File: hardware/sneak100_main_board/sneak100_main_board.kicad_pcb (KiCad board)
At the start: 2 copper layers, 68 x 72 mm, 106 parts, among them J1 Conn_01x06, J10 Conn_01x03, J11 USB_OTG, J12 Conn_01x06, J13 Conn_02x02_Odd_Even, J2 Conn_01x06, J3 Conn_01x06, J4 Conn_01x06, J5 Conn_01x03, J6 Conn_01x02, J7 Conn_01x03, J8 Conn_01x03, J9 Conn_01x03, Q1 Q_PMOS_DGS, Q2 Q_PMOS_DGS, Q3 SFH-313FA, Q4 SFH-313FA, Q5 SFH-313FA, Q6 SFH-313FA, SW1 SW_Push_SPDT, SW2 SW_Push, SW3 SW_Push, SW4 SW_Push, U1 DRV8835, U2 DRV8835, U3 DRV8835, U4 DRV8835, U5 LM1117-3.3, U6 CD4051B, U7 CD4051B, U8 TSOP4838, U9 STM32F405RGTx, Y1 8MHz

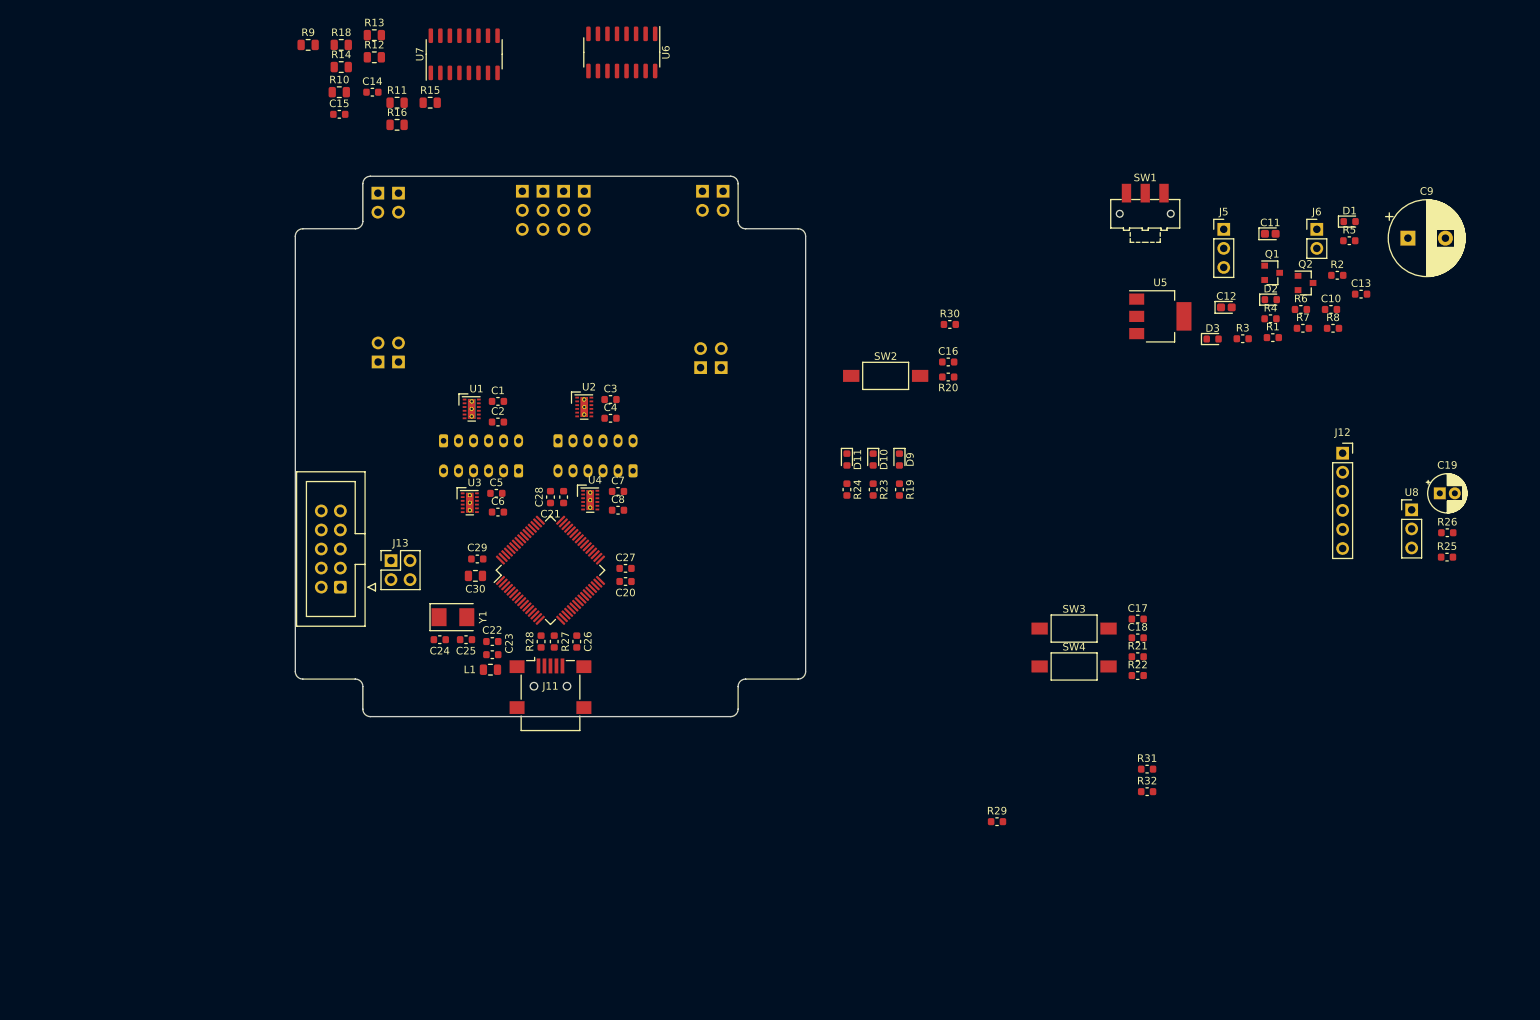
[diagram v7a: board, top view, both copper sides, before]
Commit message: delete USB, modify top hull, bigger PCB board
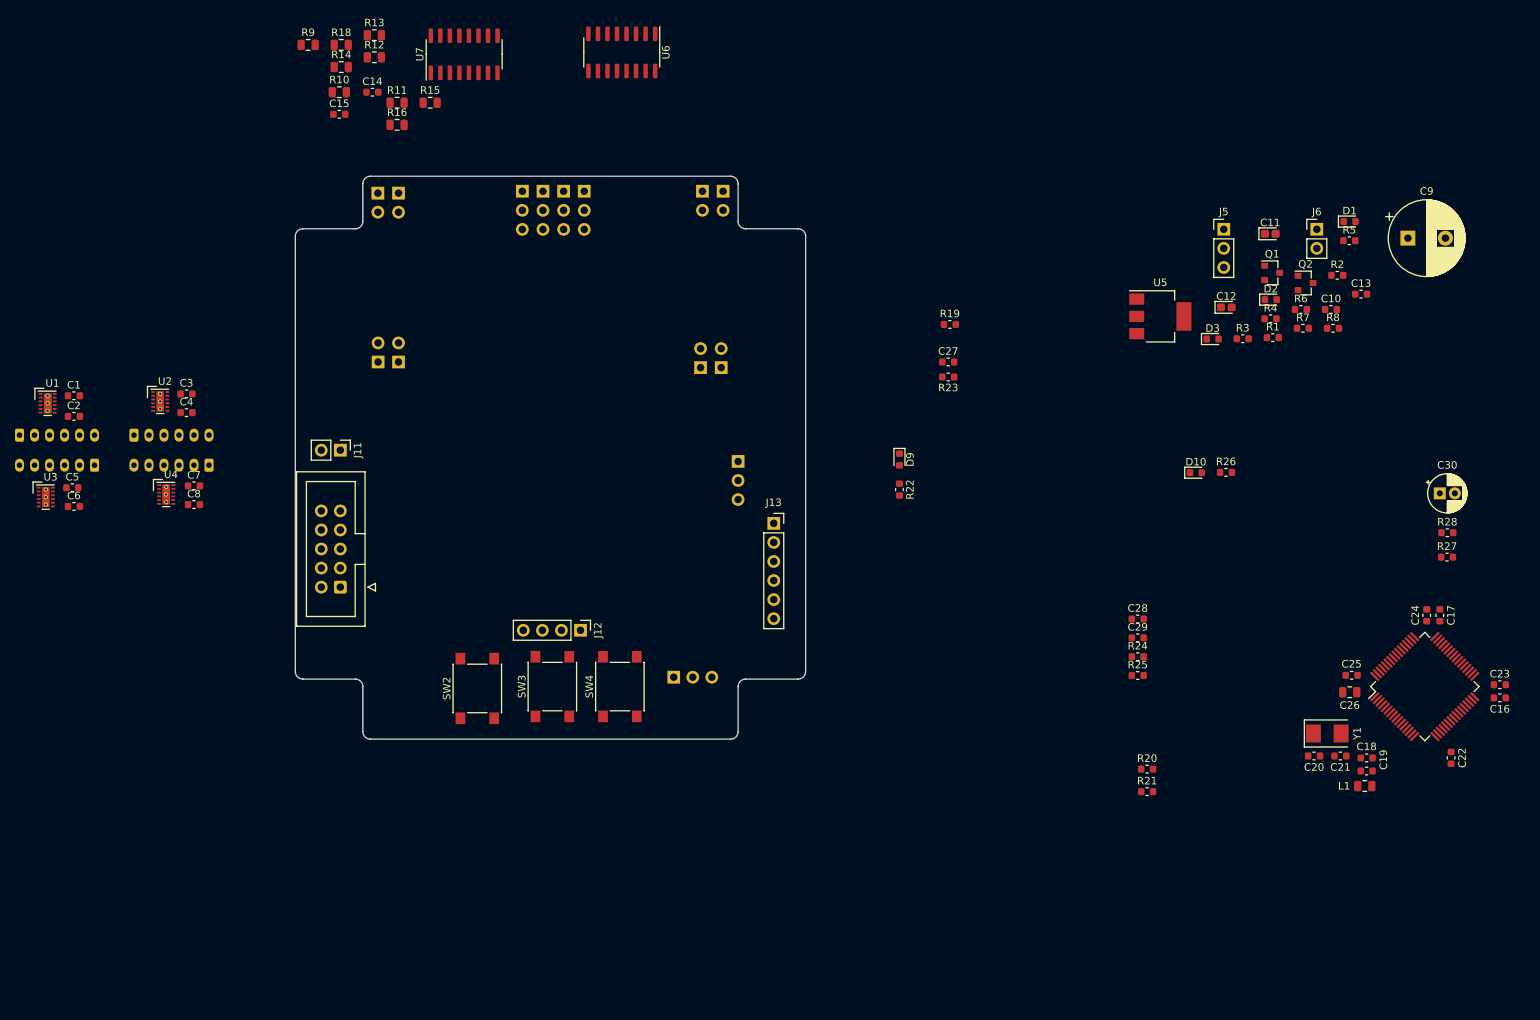
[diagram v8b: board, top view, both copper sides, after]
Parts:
- removed D11: LED, LED_SMD:LED_0603_1608Metric
- removed the J13 at (126.5, 92.7)
- removed the R23 at (190.8, 83.2)
- removed the R24 at (187.2, 83.2)
- removed the R27 at (148.2, 103.5)
- removed the R28 at (146.5, 103.5)
- removed R29: 4k7, Resistor_SMD:R_0603_1608Metric
- added J12: Conn_01x04, Connector_PinHeader_2.54mm:PinHeader_1x04_P2.54mm_Vertical, F.Cu at (151.8, 102.0)
- added R26: 340, Resistor_SMD:R_0603_1608Metric, F.Cu at (237.8, 81.0)
- J11: value USB_OTG -> Conn_01x02; footprint Connector_USB:USB_Mini-B_Lumberg_2486_01_Horizontal -> Connector_PinHeader_2.54mm:PinHeader_1x02_P2.54mm_Vertical
- SW1: footprint Button_Switch_SMD:SW_SPDT_CK-JS102011SAQN -> Connector_PinHeader_2.54mm:PinHeader_1x03_P2.54mm_Vertical; moved to B.Cu
- SW2, SW3, SW4: footprint Button_Switch_SMD:SW_SPST_FSMSM -> Button_Switch_SMD:SW_Push_1P1T_NO_6x6mm_H9.5mm
- U9: renamed from U8; moved to B.Cu
- moved C17 117.8 mm to (266.2, 100.0)
- moved C24 117.8 mm to (264.5, 100.0)
- moved C16 117.5 mm to (274.2, 111.0)
- moved C18 117.5 mm to (256.5, 119.0)
- moved C19 117.5 mm to (256.5, 120.8)
- moved C20 117.5 mm to (249.5, 118.8)
- moved C21 117.5 mm to (253.0, 118.8)
- moved C22 117.5 mm to (267.8, 119.0)
- moved C23 117.5 mm to (274.2, 109.2)
- moved C25 117.5 mm to (254.5, 108.0)
- moved C26 117.5 mm to (254.2, 110.2)
- moved L1 117.5 mm to (256.2, 122.8)
- moved U8 117.5 mm to (264.2, 109.5)
- moved Y1 117.5 mm to (251.2, 115.8)
- moved U9 90.0 mm to (172.8, 79.5), turned to 180 degrees
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- renumbered C20 to C16, C21 to C17, C22 to C18, C23 to C19, C24 to C20, C25 to C21, C26 to C22, C27 to C23, C28 to C24, C29 to C25, C30 to C26, C16 to C27, C17 to C28, C18 to C29, C19 to C30, J12 to J13, R30 to R19, R31 to R20, R32 to R21, R19 to R22, R20 to R23, R21 to R24, R22 to R25, R25 to R27, R26 to R28, U9 to U8
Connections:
- C27 pad 1: /interface/BUTTON -> /interface/BUTTON_L
- C28 pad 1: /interface/BUTTON -> /interface/BUTTON_C
- C29 pad 1: /interface/BUTTON -> /interface/BUTTON_R
- J11 pad 1: (no net) -> ST-LINK_3.3V
- J11 pad 2: Net-(J11-Pad2) -> +3V3
- R22 pad 2: /interface/LED1 -> (no net)
- R23 pad 2: /interface/BUTTON -> /interface/BUTTON_L
- R24 pad 2: /interface/BUTTON -> /interface/BUTTON_C
- R25 pad 2: /interface/BUTTON -> /interface/BUTTON_R
- SW2 pad 2: /interface/BUTTON -> /interface/BUTTON_L
- SW3 pad 2: /interface/BUTTON -> /interface/BUTTON_C
- SW4 pad 2: /interface/BUTTON -> /interface/BUTTON_R
- U8 pad 44: /controller/USB_DM -> (no net)
- U8 pad 45: /controller/USB_DP -> (no net)
- U8 pad 50: /interface/LED1 -> (no net)
- U8 pad 51: /interface/LED2 -> (no net)
- U8 pad 52: /interface/LED3 -> (no net)
- U8 pad 53: /interface/BUTTON -> (no net)
- U8 pad 60: /controller/BOOT0 -> GND
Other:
- board size 68 x 72 mm -> 68 x 75 mm
